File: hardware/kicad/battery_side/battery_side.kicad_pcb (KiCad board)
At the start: 2 copper layers, 60 x 40 mm, 45 parts, among them J1 Conn_01x02, J2 RJ45, J3 USB-OTG, J5 UART-DBG, Q1 AO3401A, Q2 AO3400A, U1 TPS62933FDRLR, U2 R-78E12-1.0, U3 SN65HVD3082E

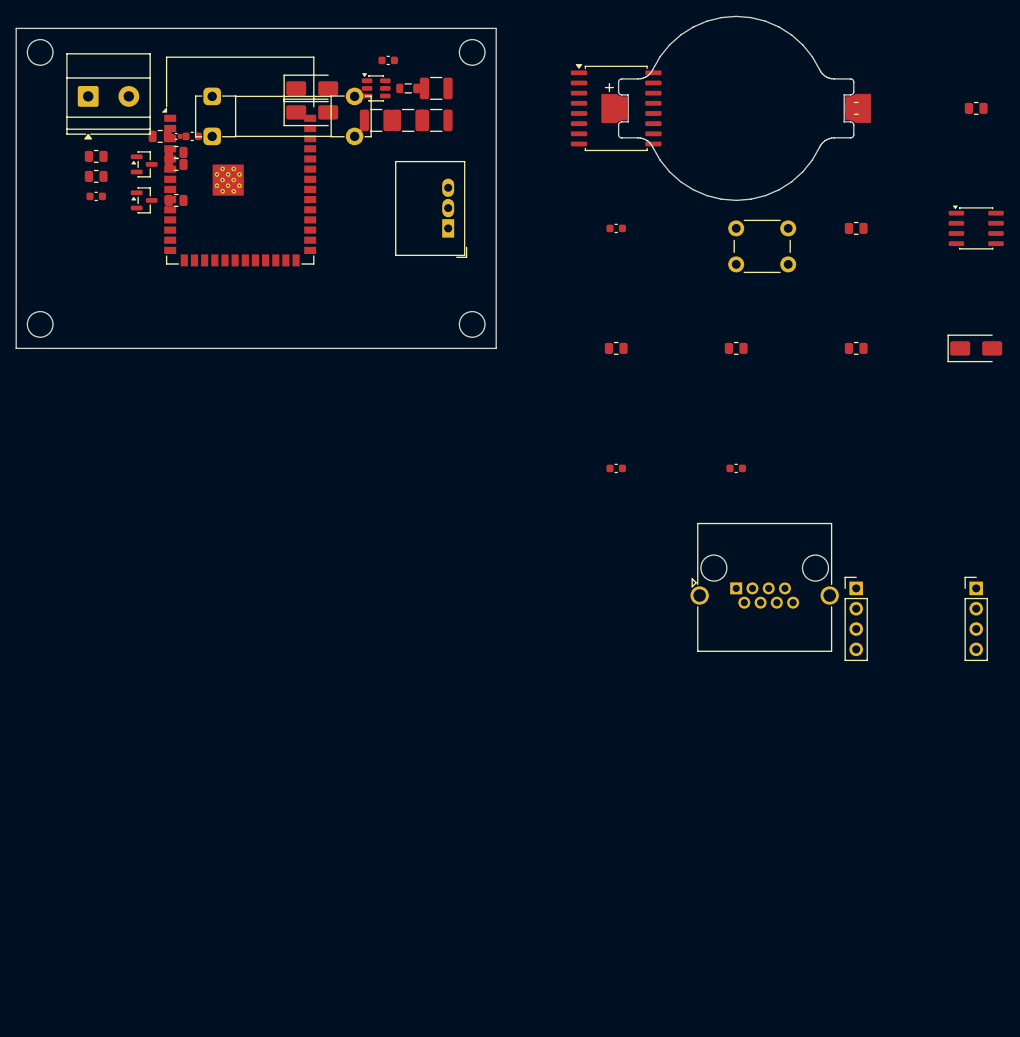
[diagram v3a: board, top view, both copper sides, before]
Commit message: hardware: CP3 iter 14 — battery-side closeout (19 components, 0 DRC errors)
Placed remaining 19 components on battery_side.kicad_pcb:

  RTC + backup       RTC1 (33, 33.5), BAT1 (17, 28) anchored so
                     Keystone Edge.Cuts stays inside 60x40 board
  I2C + RTC bypass   R8, R9, C9 — all on B.Cu, bottom strip
  Override button    BTN1 left edge F.Cu, R13+C11 on B.Cu
  RS-485             U3 (50, 16) F.Cu, R10/R11/R12 on B.Cu under
                     routing path, TVS2 F.Cu, C10 on B.Cu
  Misc decoupling    C12/C13/C14 all on B.Cu (no F.Cu space left)
  RJ45               J2 (44, 33) F.Cu, fits without overlap
  Dev headers        J3 (57, 10.5), J5 (57, 33) right edge

Layer split: 22 F.Cu / 19 B.Cu. Only way to fit 41 components on
60x40mm without overlaps.

Fixed real pad overlaps revealed when netclass_patterns triggered
shorting_items checks:
- C3/C4 spacing: moved x=52.5 -> x=54 (1210 pad needs >3.5mm pitch
  from 0805 L1/C2)
- C9 spacing: moved x=40 -> x=42.5 (clear of R9 0805 pad)

Net class definitions (Default, Power-24V, Power-12V, Power-3V3,
RS485-diff) staged in .kicad_pro but netclass_patterns NOT enabled
this iter — they trigger false-positive shorting_items across
SMD-on-different-layers and at ESP32 thermal pad. Per-net
assignment moved to CP4 with routing where track widths matter.

DRC from project dir: 0 errors, 0 unconnected, 0 footprint errors.
Top + bottom renders regenerated.

Not in this iter:
- Antenna keepout zone for MOD1 (iter 16)
- Display-side PCB (recommend separate CP)

SEMAPHORE -> codex_turn iter 15.

Co-Authored-By: Claude Opus 4.7 (1M context) <noreply@anthropic.com>
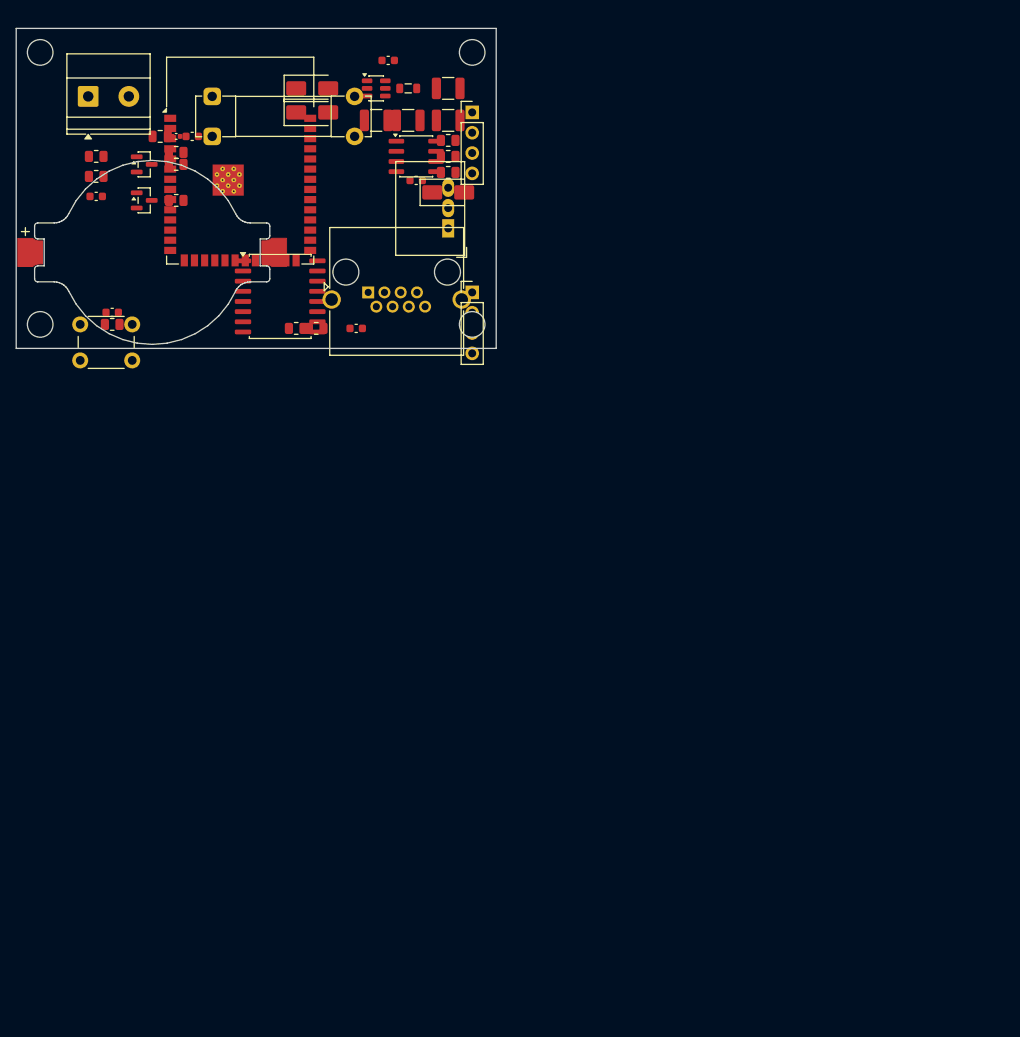
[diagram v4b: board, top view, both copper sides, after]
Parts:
- C10, C11, C9, R10, R11, R12, R13, R8, R9: moved to B.Cu
- moved R13 93.8 mm to (12.0, 37.0)
- moved R9 87.0 mm to (37.5, 37.5)
- moved BTN1 82.9 mm to (8.00, 37.0)
- moved C11 80.4 mm to (12.0, 35.5)
- moved J3 76.4 mm to (57.0, 10.5)
- moved R8 75.2 mm to (35.0, 37.5)
- moved BAT1 75.2 mm to (17.0, 28.0)
- moved J5 73.1 mm to (57.0, 33.0)
- moved U3 70.6 mm to (50.0, 16.0)
- moved TVS2 68.8 mm to (54.0, 20.5)
- moved J2 59.0 mm to (44.0, 33.0)
- moved R12 55.5 mm to (54.0, 18.0)
- moved RTC1 48.1 mm to (33.0, 33.5)
- moved C10 43.8 mm to (50.0, 19.0)
- moved R11 43.3 mm to (54.0, 16.0)
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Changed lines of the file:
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@@
   (net 26 "V_BAT_RTC")
   (footprint "volthium:BatteryHolder_Keystone_1057_1x2032" (version 20260206) (generator pcbnew) (layer "F.Cu")
-    (at 90.0 10.0 0)
+    (at 17.0 28.0 0)
     (descr "SMT (Auto-In/Ultra-Low) Holder for 2032 Cell, 33.2 x 23.9mm, 2mm height above PCB, https://www.keyelco.com/userAssets/file/M65p4.pdf")
     (tags "Keystone type 1057 coin cell holder CR2032")
@@
   )
   (footprint "volthium:SW_PUSH_6mm" (version 20260206) (generator pcbnew) (layer "F.Cu")
-    (at 90.0 25.0 0)
+    (at 8.0 37.0 0)
     (descr "Generic 6mm SW tactile push button")
     (tags "tact sw push 6mm")
@@
     )
   )
-  (footprint "volthium:C_0603_1608Metric" (version 20260206) (generator kicad-footprint-generator) (layer "F.Cu")
-    (at 75.0 55.0 0)
+  (footprint "volthium:C_0603_1608Metric" (version 20260206) (generator kicad-footprint-generator) (layer "B.Cu")
+    (at 50.0 19.0 0)
     (descr "Capacitor SMD 0603 (1608 Metric), square (rectangular) end terminal, IPC-7351 nominal, (Body size source: IPC-SM-782 page 76, https://www.pcb-3d.com/wordpress/wp-content/uploads/ipc-sm-782a_amendment_1_and_2.pdf)")
     (tags "capacitor")
@@
     )
   )
-  (footprint "volthium:C_0603_1608Metric" (version 20260206) (generator kicad-footprint-generator) (layer "F.Cu")
-    (at 90.0 55.0 0)
+  (footprint "volthium:C_0603_1608Metric" (version 20260206) (generator kicad-footprint-generator) (layer "B.Cu")
+    (at 12.0 35.5 0)
     (descr "Capacitor SMD 0603 (1608 Metric), square (rectangular) end terminal, IPC-7351 nominal, (Body size source: IPC-SM-782 page 76, https://www.pcb-3d.com/wordpress/wp-content/uploads/ipc-sm-782a_amendment_1_and_2.pdf)")
     (tags "capacitor")
@@
   )
   (footprint "volthium:C_1210_3225Metric" (version 20260206) (generator kicad-footprint-generator) (layer "F.Cu")
-    (at 52.5 7.5 0)
+    (at 54.0 7.5 0)
     (descr "Capacitor SMD 1210 (3225 Metric), square (rectangular) end terminal, IPC-7351 nominal, (Body size source: IPC-SM-782 page 76, https://www.pcb-3d.com/wordpress/wp-content/uploads/ipc-sm-782a_amendment_1_and_2.pdf)")
     (tags "capacitor")
@@
   )
   (footprint "volthium:C_1210_3225Metric" (version 20260206) (generator kicad-footprint-generator) (layer "F.Cu")
-    (at 52.5 11.5 0)
+    (at 54.0 11.5 0)
     (descr "Capacitor SMD 1210 (3225 Metric), square (rectangular) end terminal, IPC-7351 nominal, (Body size source: IPC-SM-782 page 76, https://www.pcb-3d.com/wordpress/wp-content/uploads/ipc-sm-782a_amendment_1_and_2.pdf)")
     (tags "capacitor")
@@
     )
   )
-  (footprint "volthium:C_0603_1608Metric" (version 20260206) (generator kicad-footprint-generator) (layer "F.Cu")
-    (at 75.0 25.0 0)
+  (footprint "volthium:C_0603_1608Metric" (version 20260206) (generator kicad-footprint-generator) (layer "B.Cu")
+    (at 42.5 37.5 0)
     (descr "Capacitor SMD 0603 (1608 Metric), square (rectangular) end terminal, IPC-7351 nominal, (Body size source: IPC-SM-782 page 76, https://www.pcb-3d.com/wordpress/wp-content/uploads/ipc-sm-782a_amendment_1_and_2.pdf)")
     (tags "capacitor")
@@
   )
   (footprint "volthium:RJ45_Amphenol_RJHSE5380" (version 20260206) (generator pcbnew) (layer "F.Cu")
-    (at 90.0 70.0 0)
+    (at 44.0 33.0 0)
     (descr "Shielded, https://www.amphenolcanada.com/ProductSearch/drawings/AC/RJHSE538X.pdf")
     (tags "RJ45 8p8c ethernet cat5")
@@
   )
   (footprint "volthium:PinHeader_1x04_P2.54mm_Vertical" (version 20260206) (generator kicad-footprint-generator) (layer "F.Cu")
-    (at 105.0 70.0 0)
+    (at 57.0 10.5 0)
     (descr "Through hole straight pin header, 1x04, 2.54mm pitch, single row")
     (tags "Through hole pin header THT 1x04 2.54mm single row")
@@
   )
   (footprint "volthium:PinHeader_1x04_P2.54mm_Vertical" (version 20260206) (generator kicad-footprint-generator) (layer "F.Cu")
-    (at 120.0 70.0 0)
+    (at 57.0 33.0 0)
     (descr "Through hole straight pin header, 1x04, 2.54mm pitch, single row")
     (tags "Through hole pin header THT 1x04 2.54mm single row")
@@
     )
   )
-  (footprint "volthium:R_0805_2012Metric" (version 20260206) (generator kicad-footprint-generator) (layer "F.Cu")
-    (at 75.0 40.0 0)
+  (footprint "volthium:R_0805_2012Metric" (version 20260206) (generator kicad-footprint-generator) (layer "B.Cu")
+    (at 54.0 14.0 0)
     (descr "Resistor SMD 0805 (2012 Metric), square (rectangular) end terminal, IPC-7351 nominal, (Body size source: IPC-SM-782 page 72, https://www.pcb-3d.com/wordpress/wp-content/uploads/ipc-sm-782a_amendment_1_and_2.pdf)")
     (tags "resistor")
@@
     )
   )
-  (footprint "volthium:R_0805_2012Metric" (version 20260206) (generator kicad-footprint-generator) (layer "F.Cu")
-    (at 90.0 40.0 0)
+  (footprint "volthium:R_0805_2012Metric" (version 20260206) (generator kicad-footprint-generator) (layer "B.Cu")
+    (at 54.0 16.0 0)
     (descr "Resistor SMD 0805 (2012 Metric), square (rectangular) end terminal, IPC-7351 nominal, (Body size source: IPC-SM-782 page 72, https://www.pcb-3d.com/wordpress/wp-content/uploads/ipc-sm-782a_amendment_1_and_2.pdf)")
     (tags "resistor")
@@
     )
   )
-  (footprint "volthium:R_0805_2012Metric" (version 20260206) (generator kicad-footprint-generator) (layer "F.Cu")
-    (at 105.0 40.0 0)
+  (footprint "volthium:R_0805_2012Metric" (version 20260206) (generator kicad-footprint-generator) (layer "B.Cu")
+    (at 54.0 18.0 0)
     (descr "Resistor SMD 0805 (2012 Metric), square (rectangular) end terminal, IPC-7351 nominal, (Body size source: IPC-SM-782 page 72, https://www.pcb-3d.com/wordpress/wp-content/uploads/ipc-sm-782a_amendment_1_and_2.pdf)")
     (tags "resistor")
@@
     )
   )
-  (footprint "volthium:R_0805_2012Metric" (version 20260206) (generator kicad-footprint-generator) (layer "F.Cu")
-    (at 105.0 25.0 0)
+  (footprint "volthium:R_0805_2012Metric" (version 20260206) (generator kicad-footprint-generator) (layer "B.Cu")
+    (at 12.0 37.0 0)
     (descr "Resistor SMD 0805 (2012 Metric), square (rectangular) end terminal, IPC-7351 nominal, (Body size source: IPC-SM-782 page 72, https://www.pcb-3d.com/wordpress/wp-content/uploads/ipc-sm-782a_amendment_1_and_2.pdf)")
     (tags "resistor")
@@
     )
   )
-  (footprint "volthium:R_0805_2012Metric" (version 20260206) (generator kicad-footprint-generator) (layer "F.Cu")
-    (at 105.0 10.0 0)
+  (footprint "volthium:R_0805_2012Metric" (version 20260206) (generator kicad-footprint-generator) (layer "B.Cu")
+    (at 35.0 37.5 0)
     (descr "Resistor SMD 0805 (2012 Metric), square (rectangular) end terminal, IPC-7351 nominal, (Body size source: IPC-SM-782 page 72, https://www.pcb-3d.com/wordpress/wp-content/uploads/ipc-sm-782a_amendment_1_and_2.pdf)")
     (tags "resistor")
@@
     )
   )
-  (footprint "volthium:R_0805_2012Metric" (version 20260206) (generator kicad-footprint-generator) (layer "F.Cu")
-    (at 120.0 10.0 0)
+  (footprint "volthium:R_0805_2012Metric" (version 20260206) (generator kicad-footprint-generator) (layer "B.Cu")
+    (at 37.5 37.5 0)
     (descr "Resistor SMD 0805 (2012 Metric), square (rectangular) end terminal, IPC-7351 nominal, (Body size source: IPC-SM-782 page 72, https://www.pcb-3d.com/wordpress/wp-content/uploads/ipc-sm-782a_amendment_1_and_2.pdf)")
     (tags "resistor")
@@
   )
   (footprint "volthium:SOIC-16W_7.5x10.3mm_P1.27mm" (version 20260206) (generator kicad-footprint-generator) (layer "F.Cu")
-    (at 75.0 10.0 0)
+    (at 33.0 33.5 0)
     (descr "SOIC, 16 Pin (JEDEC MS-013AA, https://www.analog.com/media/en/package-pcb-resources/package/pkg_pdf/soic_wide-rw/rw_16.pdf)")
     (tags "SOIC SO")
@@
   )
   (footprint "volthium:D_SMA" (version 20260206) (generator pcbnew) (layer "F.Cu")
-    (at 120.0 40.0 0)
+    (at 54.0 20.5 0)
     (descr "Diode SMA (DO-214AC)")
     (tags "Diode SMA (DO-214AC)")
@@
   )
   (footprint "volthium:SOIC-8_3.9x4.9mm_P1.27mm" (version 20260206) (generator kicad-footprint-generator) (layer "F.Cu")
-    (at 120.0 25.0 0)
+    (at 50.0 16.0 0)
     (descr "SOIC, 8 Pin (JEDEC MS-012AA, https://www.analog.com/media/en/package-pcb-resources/package/pkg_pdf/soic_narrow-r/r_8.pdf)")
     (tags "SOIC SO")

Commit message: hardware: CP3 iter 16 — Findings 04 + 05 (net classes, RTC1/J2 clash)
Finding 05 (RTC1/J2 hole_clearance) ACCEPTED, fixed
==================================================

RTC1 moved from (33, 33.5) to (30, 35).
  x: right-edge pin now at x=34.65, 4.78mm clear of J2 shield (39.43)
  y: top edge now at y=31.25, 2.25mm clear of MOD1 bottom pad row

Verification (project dir):
  kicad-cli pcb drc --severity-error battery_side.kicad_pcb
  -> Found 0 violations, 0 unconnected, 0 footprint errors

Finding 04 (CP1 net classes) PARTIAL, with surfaced tradeoff
============================================================

CP1 §11.3 class names now present in battery_side.kicad_pro
net_settings.classes: Default, Power-24V, Power-12V, Power-3V3,
RS485-diff.

Numeric values (clearance, track_width, via_diameter, via_drill +
netclass_patterns) stored as JSON comments in the same file under
_intended_classes_cp4 / _intended_patterns_cp4 keys. CP4 routing
reinstates them with KiCad's checker bindings.

Why not bind the numerics now: tested with full clearance values
on Default class — DRC reports 33 errors between adjacent SMD pads
on different layers, ESP32 thermal pad fingers, and tight bypass
arrangements. These are real placement-vs-routing tradeoffs that
CP4 resolves through track routing + copper pours, not by moving
footprints further apart.

Tradeoff surfaced in cp3_placement.md §10.16. If Codex prefers
"full numerics now + carry 33 DRC errors to CP4", easy switch.

Antenna keepout zone still deferred to iter 18.

SEMAPHORE -> codex_turn iter 17.

Co-Authored-By: Claude Opus 4.7 (1M context) <noreply@anthropic.com>
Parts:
- moved RTC1 3.35 mm to (30.0, 35.0)
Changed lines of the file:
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@@
   )
   (footprint "volthium:SOIC-16W_7.5x10.3mm_P1.27mm" (version 20260206) (generator kicad-footprint-generator) (layer "F.Cu")
-    (at 33.0 33.5 0)
+    (at 30.0 35.0 0)
     (descr "SOIC, 16 Pin (JEDEC MS-013AA, https://www.analog.com/media/en/package-pcb-resources/package/pkg_pdf/soic_wide-rw/rw_16.pdf)")
     (tags "SOIC SO")

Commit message: hardware: CP3 iter 20 — Option A executed (ESP32-S3-WROOM-1 -> -1U)
User picked Option A from iter 18's antenna keepout decision.
Switched ESP32-S3-WROOM-1 (PCB antenna + 48x21mm safety keepout) to
ESP32-S3-WROOM-1U (external U.FL antenna, zero keepout).

Schematic changes (build_schematics.py):
  RF_Module:ESP32-S3-WROOM-1 -> RF_Module:ESP32-S3-WROOM-1U
  (Footprint field only; same symbol — KiCad's RF_Module library
  has one ESP32-S3-WROOM-1 symbol used by both variants.)

PCB changes (build_pcbs.py):
  STOCK_FOOTPRINTS updated; --rebuild-footprints repopulated cache
  MOD1 anchor (28, 16.5) -> (28, 19.65)

The +3.15mm y shift compensates for the -1U footprint's anchor
sitting 3.15mm offset from pad-bbox center relative to the -1
footprint. Result: all module pin positions in absolute board
coords STAY IDENTICAL to pre-swap. All dependent placements
(bypass row C6/C7/C8 under pin 2, R7 EN-pullup at pin 3, hard-cut
Q1-Q4 around pin 4 PWR_EN, RTC1) remain valid without further
moves.

Verification:
  MOD1 libId:        volthium:ESP32-S3-WROOM-1U
  MOD1 anchor:       (28, 19.65)
  MOD1 pin 2 abs:    (19.25, 12.51)   unchanged
  MOD1 keepout zones: 0                (was 1: 48x21mm)
  ERC both boards:   0/0
  DRC project dir:   0 errors
  Netlist diff: 1 footprint string change only; topology preserved

BOM: +uFL pigtail + external antenna (~$3-5). External antenna
mounts to project box wall — better RF perf than PCB antenna would
have given even without the keepout.

.kicad_pro had to be re-applied after a linter (kicad-cli pcb
upgrade or save-normalize) stripped the rule_severities overrides
and named net classes. Restored: DRC overrides + 5 CP1 §11.3
classes + _intended_*cp4 numerics.

SEMAPHORE -> codex_turn iter 21.

Co-Authored-By: Claude Opus 4.7 (1M context) <noreply@anthropic.com>
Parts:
- MOD1: footprint volthium:ESP32-S3-WROOM-1 -> volthium:ESP32-S3-WROOM-1U
- moved MOD1 3.15 mm to (28.0, 19.6)
